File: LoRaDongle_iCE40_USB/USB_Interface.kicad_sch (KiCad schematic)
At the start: 25 parts, among them IC1 93LC56BT-I_OT, U2 FT232H, Y1 Crystal_GND24_Small

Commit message: updating unconnected traces
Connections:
- net UBS_D+ renamed USB_D+
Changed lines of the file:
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@@
     )
   )
-  (hierarchical_label "UBS_D+" (shape input) (at 140.97 58.42 180)
+  (hierarchical_label "USB_D+" (shape input) (at 140.97 58.42 180)
     (effects (font (size 1.27 1.27)) (justify right))
   )

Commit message: updating symbol details
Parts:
- C10: Manufacturer (none) -> Murata Electronics; Manufacturer Part Number (none) -> GRM155R71H103KA88J; Package (none) -> 0402; Type (none) -> SMD
- C11, C17, C7: footprint Capacitor_SMD:C_0603_1608Metric_Pad1.08x0.95mm_HandSolder -> Capacitor_SMD:C_0402_1005Metric_Pad0.74x0.62mm_HandSolder; Manufacturer (none) -> Murata Electronics; Manufacturer Part Number (none) -> GRM155C80J475MEAAD; Package (none) -> 0402; Type (none) -> SMD
- C12, C13, C16, C18, C19, C20, C21, C22, C8, C9: Manufacturer (none) -> Murata Electronics; Manufacturer Part Number (none) -> GCM155R71C104KA55J; Package (none) -> 0402; Type (none) -> SMD
- C14, C15: Manufacturer Part Number (none) -> Need to Find; Package (none) -> 0603; Type (none) -> SMD
- FB2, FB3: Manufacturer Part Number (none) -> BLM18AG601SN1D; Package (none) -> 0603; Type (none) -> SMD
- IC1: Manufacturer (none) -> Microchip; Manufacturer Part Number (none) -> 93LC56BT-I/OT; Package (none) -> SOT23-6; Type (none) -> SMD
- U2: Manufacturer (none) -> FTDI, Future Technology Devices International Ltd; Manufacturer Part Number (none) -> FT232HL; Package (none) -> LQFP-48; Type (none) -> SMD
- Y1: Manufacturer (none) -> Abracon LLC; Manufacturer Part Number (none) -> ABM8-12.000MHZ-B2-T; Package (none) -> 4 Pin Crystal; Type (none) -> SMD

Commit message: updated BOM
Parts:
- C14, C15: Manufacturer (none) -> Murata Electronics; Manufacturer Part Number Need to Find -> GRM1885C1H270JA01D
- R10, R8: Manufacturer (none) -> Stackpole Electronics Inc; Manufacturer Part Number (none) -> RMCF0402FT10K0
- R11: Manufacturer (none) -> Stackpole Electronics Inc; Manufacturer Part Number (none) -> RMCF0402FT12K0
- R9: Manufacturer (none) -> Stackpole Electronics Inc; Manufacturer Part Number (none) -> RMCF0402FT2K00
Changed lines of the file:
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@@
+      (effects (font (size 1.27 1.27)) hide)
+    )
+    (property "Description" "RES 10K OHM 1% 1/16W 0402" (id 4) (at 133.35 68.58 0)
+      (effects (font (size 1.27 1.27)) hide)
+    )
+    (property "Manufacturer" "Stackpole Electronics Inc" (id 5) (at 133.35 68.58 0)
+      (effects (font (size 1.27 1.27)) hide)
+    )
+    (property "Manufacturer Part Number" "RMCF0402FT12K0" (id 6) (at 133.35 68.58 0)
       (effects (font (size 1.27 1.27)) hide)
     )
@@
       (effects (font (size 1.27 1.27)) hide)
     )
+    (property "Description" "RES 2K OHM 1% 1/16W 0402" (id 4) (at 104.14 81.28 0)
+      (effects (font (size 1.27 1.27)) hide)
+    )
+    (property "Manufacturer" "Stackpole Electronics Inc" (id 5) (at 104.14 81.28 0)
+      (effects (font (size 1.27 1.27)) hide)
+    )
+    (property "Manufacturer Part Number" "RMCF0402FT2K00" (id 6) (at 104.14 81.28 0)
+      (effects (font (size 1.27 1.27)) hide)
+    )
     (pin "1")
     (pin "2")
@@
       (effects (font (size 1.27 1.27)) hide)
     )
+    (property "Description" "RES 10K OHM 1% 1/16W 0402" (id 4) (at 105.41 88.9 0)
+      (effects (font (size 1.27 1.27)) hide)
+    )
+    (property "Manufacturer" "Stackpole Electronics Inc" (id 5) (at 105.41 88.9 0)
+      (effects (font (size 1.27 1.27)) hide)
+    )
+    (property "Manufacturer Part Number" "RMCF0402FT10K0" (id 6) (at 105.41 88.9 0)
+      (effects (font (size 1.27 1.27)) hide)
+    )
     (pin "1")
     (pin "2")
@@
       (effects (font (size 1.27 1.27)) hide)
     )
-    (property "Manufacturer Part Number" "Need to Find " (id 4) (at 129.54 93.98 0)
+    (property "Manufacturer Part Number" "GRM1885C1H270JA01D" (id 4) (at 129.54 93.98 0)
       (effects (font (size 1.27 1.27)) hide)
     )
@@
     )
     (property "Type" "SMD" (id 6) (at 129.54 93.98 0)
+      (effects (font (size 1.27 1.27)) hide)
+    )
+    (property "Description" "CAP CER 27PF 50V C0G/NP0 0603" (id 7) (at 129.54 93.98 0)
+      (effects (font (size 1.27 1.27)) hide)
+    )
+    (property "Manufacturer" "Murata Electronics" (id 8) (at 129.54 93.98 0)
       (effects (font (size 1.27 1.27)) hide)
     )
@@
       (effects (font (size 1.27 1.27)) hide)
     )
-    (property "Manufacturer Part Number" "Need to Find " (id 4) (at 129.54 83.82 0)
+    (property "Manufacturer Part Number" "GRM1885C1H270JA01D" (id 4) (at 129.54 83.82 0)
       (effects (font (size 1.27 1.27)) hide)
     )
@@
     )
     (property "Type" "SMD" (id 6) (at 129.54 83.82 0)
+      (effects (font (size 1.27 1.27)) hide)
+    )
+    (property "Description" "CAP CER 27PF 50V C0G/NP0 0603" (id 7) (at 129.54 83.82 0)
+      (effects (font (size 1.27 1.27)) hide)
+    )
+    (property "Manufacturer" "Murata Electronics" (id 8) (at 129.54 83.82 0)
       (effects (font (size 1.27 1.27)) hide)
     )
@@
       (effects (font (size 1.27 1.27)) hide)
     )
+    (property "Description" "RES 10K OHM 1% 1/16W 0402" (id 4) (at 87.63 57.15 0)
+      (effects (font (size 1.27 1.27)) hide)
+    )
+    (property "Manufacturer" "Stackpole Electronics Inc" (id 5) (at 87.63 57.15 0)
+      (effects (font (size 1.27 1.27)) hide)
+    )
+    (property "Manufacturer Part Number" "RMCF0402FT10K0" (id 6) (at 87.63 57.15 0)
+      (effects (font (size 1.27 1.27)) hide)
+    )

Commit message: generate raw bom csv from kicad
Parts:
- R10, R11, R8, R9: Package (none) -> 0402
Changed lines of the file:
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@@
+      (effects (font (size 1.27 1.27)) hide)
+    )
+    (property "Package" "0402" (id 7) (at 133.35 68.58 0)
       (effects (font (size 1.27 1.27)) hide)
     )
@@
       (effects (font (size 1.27 1.27)) hide)
     )
+    (property "Package" "0402" (id 7) (at 104.14 81.28 0)
+      (effects (font (size 1.27 1.27)) hide)
+    )
     (pin "1")
     (pin "2")
@@
       (effects (font (size 1.27 1.27)) hide)
     )
+    (property "Package" "0402" (id 7) (at 105.41 88.9 0)
+      (effects (font (size 1.27 1.27)) hide)
+    )
     (pin "1")
     (pin "2")
@@
       (effects (font (size 1.27 1.27)) hide)
     )
+    (property "Package" "0402" (id 7) (at 87.63 57.15 0)
+      (effects (font (size 1.27 1.27)) hide)
+    )

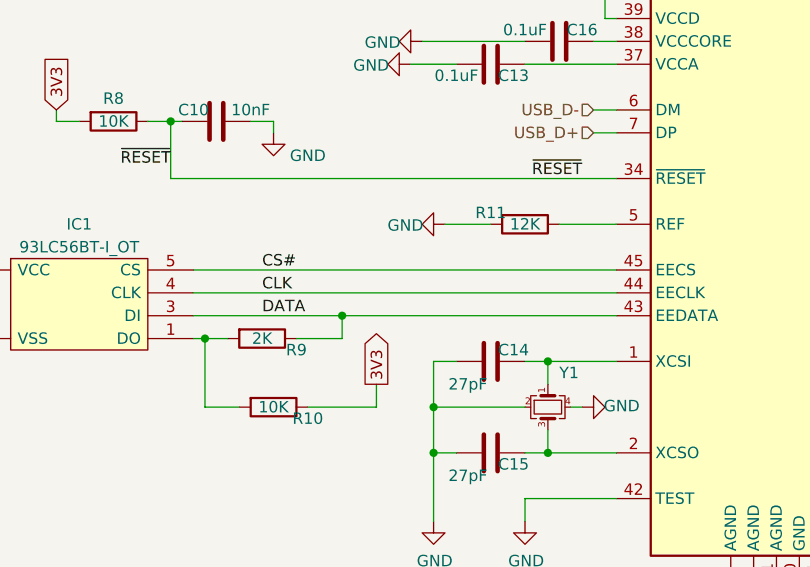
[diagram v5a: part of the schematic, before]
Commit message: added usb flash testpoints & jumper for fpga oscillator
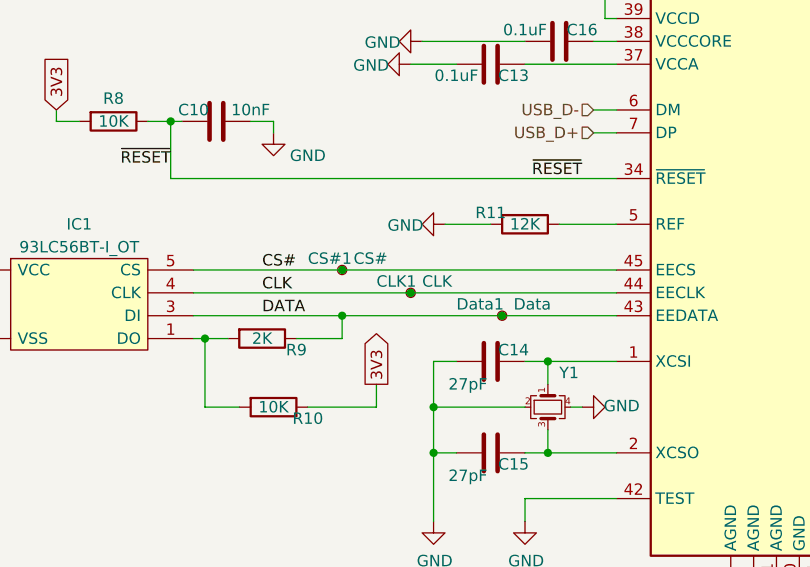
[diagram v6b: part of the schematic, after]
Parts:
- added CLK1: CLK, TestPoint:TestPoint_Pad_D1.0mm, symbol Connector:TestPoint_Small
- added CS#1: CS#, TestPoint:TestPoint_Pad_D1.0mm, symbol Connector:TestPoint_Small
- added Data1: Data, TestPoint:TestPoint_Pad_D1.0mm, symbol Connector:TestPoint_Small
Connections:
- net CLK: now also CLK1.1
- net CS#: now also CS#1.1
- net DATA: now also Data1.1
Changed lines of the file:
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@@
   (junction (at 172.72 144.78) (diameter 0) (color 0 0 0 0)
   )
+  (junction (at 120.65 76.2) (diameter 0) (color 0 0 0 0)
+  )
   (junction (at 64.77 73.66) (diameter 0) (color 0 0 0 0)
   )
@@
   (junction (at 142.24 40.64) (diameter 0) (color 0 0 0 0)
   )
+  (junction (at 135.89 93.98) (diameter 0) (color 0 0 0 0)
+  )
+  (junction (at 163.83 111.76) (diameter 0) (color 0 0 0 0)
+  )
+  (junction (at 166.37 111.76) (diameter 0) (color 0 0 0 0)
+  )
   (junction (at 113.03 78.74) (diameter 0) (color 0 0 0 0)
   )
-  (junction (at 135.89 93.98) (diameter 0) (color 0 0 0 0)
-  )
-  (junction (at 163.83 111.76) (diameter 0) (color 0 0 0 0)
-  )
-  (junction (at 166.37 111.76) (diameter 0) (color 0 0 0 0)
-  )
   (junction (at 168.91 111.76) (diameter 0) (color 0 0 0 0)
   )
+  (junction (at 130.81 78.74) (diameter 0) (color 0 0 0 0)
+  )
   (junction (at 118.11 144.78) (diameter 0) (color 0 0 0 0)
+  )
+  (junction (at 113.03 73.66) (diameter 0) (color 0 0 0 0)
   )
   (junction (at 158.75 111.76) (diameter 0) (color 0 0 0 0)
@@
     (stroke (width 0) (type default) (color 0 0 0 0))
   )
+  (wire (pts (xy 96.52 73.66) (xy 113.03 73.66))
+    (stroke (width 0) (type default) (color 0 0 0 0))
+  )
   (wire (pts (xy 187.96 144.78) (xy 189.23 144.78))
     (stroke (width 0) (type default) (color 0 0 0 0))
@@
     (stroke (width 0) (type default) (color 0 0 0 0))
   )
+  (wire (pts (xy 96.52 76.2) (xy 120.65 76.2))
+    (stroke (width 0) (type default) (color 0 0 0 0))
+  )
   (wire (pts (xy 133.35 99.06) (xy 143.51 99.06))
     (stroke (width 0) (type default) (color 0 0 0 0))
@@
     (stroke (width 0) (type default) (color 0 0 0 0))
   )
+  (wire (pts (xy 120.65 76.2) (xy 143.51 76.2))
+    (stroke (width 0) (type default) (color 0 0 0 0))
+  )
   (wire (pts (xy 156.21 109.22) (xy 156.21 111.76))
     (stroke (width 0) (type default) (color 0 0 0 0))
@@
     (stroke (width 0) (type default) (color 0 0 0 0))
   )
+  (wire (pts (xy 113.03 78.74) (xy 130.81 78.74))
+    (stroke (width 0) (type default) (color 0 0 0 0))
+  )
   (wire (pts (xy 124.46 68.58) (xy 129.54 68.58))
     (stroke (width 0) (type default) (color 0 0 0 0))
@@
     (stroke (width 0) (type default) (color 0 0 0 0))
   )
-  (wire (pts (xy 96.52 76.2) (xy 143.51 76.2))
-    (stroke (width 0) (type default) (color 0 0 0 0))
-  )
   (wire (pts (xy 143.51 58.42) (xy 140.97 58.42))
     (stroke (width 0) (type default) (color 0 0 0 0))
@@
     (stroke (width 0) (type default) (color 0 0 0 0))
   )
+  (wire (pts (xy 130.81 78.74) (xy 143.51 78.74))
+    (stroke (width 0) (type default) (color 0 0 0 0))
+  )
   (wire (pts (xy 172.72 144.78) (xy 181.61 144.78))
     (stroke (width 0) (type default) (color 0 0 0 0))
@@
     (stroke (width 0) (type default) (color 0 0 0 0))
   )
-  (wire (pts (xy 113.03 78.74) (xy 143.51 78.74))
-    (stroke (width 0) (type default) (color 0 0 0 0))
-  )
   (wire (pts (xy 96.52 81.28) (xy 97.79 81.28))
     (stroke (width 0) (type default) (color 0 0 0 0))
   )
-  (wire (pts (xy 96.52 73.66) (xy 143.51 73.66))
-    (stroke (width 0) (type default) (color 0 0 0 0))
-  )
   (wire (pts (xy 72.39 144.78) (xy 68.58 144.78))
     (stroke (width 0) (type default) (color 0 0 0 0))
@@
   )
   (wire (pts (xy 41.91 132.08) (xy 41.91 134.62))
+    (stroke (width 0) (type default) (color 0 0 0 0))
+  )
+  (wire (pts (xy 113.03 73.66) (xy 143.51 73.66))
     (stroke (width 0) (type default) (color 0 0 0 0))
   )
@@
       (effects (font (size 1.27 1.27)) hide)
     )
+    (pin "1")
+  )
+  (symbol (lib_id "Connector:TestPoint_Small") (at 113.03 73.66 0) (unit 1)
+    (in_bom yes) (on_board yes)
+    (property "Reference" "CS#1" (id 0) (at 109.22 72.39 0)
+      (effects (font (size 1.27 1.27)) (justify left))
+    )
+    (property "Value" "CS#" (id 1) (at 114.3 72.39 0)
+      (effects (font (size 1.27 1.27)) (justify left))
+    )
+    (property "Footprint" "TestPoint:TestPoint_Pad_D1.0mm" (id 2) (at 118.11 73.66 0)
+      (effects (font (size 1.27 1.27)) hide)
+    )
+    (property "Datasheet" "~" (id 3) (at 118.11 73.66 0)
+      (effects (font (size 1.27 1.27)) hide)
+    )
+    (pin "1")
+  )
+  (symbol (lib_id "Connector:TestPoint_Small") (at 130.81 78.74 0) (unit 1)
+    (in_bom yes) (on_board yes)
+    (property "Reference" "Data1" (id 0) (at 125.73 77.47 0)
+      (effects (font (size 1.27 1.27)) (justify left))
+    )
+    (property "Value" "Data" (id 1) (at 132.08 77.47 0)
+      (effects (font (size 1.27 1.27)) (justify left))
+    )
+    (property "Footprint" "TestPoint:TestPoint_Pad_D1.0mm" (id 2) (at 135.89 78.74 0)
+      (effects (font (size 1.27 1.27)) hide)
+    )
+    (property "Datasheet" "~" (id 3) (at 135.89 78.74 0)
+      (effects (font (size 1.27 1.27)) hide)
+    )
+    (pin "1")
+  )
+  (symbol (lib_id "Connector:TestPoint_Small") (at 120.65 76.2 0) (unit 1)
+    (in_bom yes) (on_board yes)
+    (property "Reference" "CLK1" (id 0) (at 116.84 74.93 0)
+      (effects (font (size 1.27 1.27)) (justify left))
+    )
+    (property "Value" "CLK" (id 1) (at 121.92 74.93 0)
+      (effects (font (size 1.27 1.27)) (justify left))
+    )
+    (property "Footprint" "TestPoint:TestPoint_Pad_D1.0mm" (id 2) (at 125.73 76.2 0)
+      (effects (font (size 1.27 1.27)) hide)
+    )
+    (property "Datasheet" "~" (id 3) (at 125.73 76.2 0)
+      (effects (font (size 1.27 1.27)) hide)
+    )

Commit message: updating silkscreen
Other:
- company: (none) -> Mark Njoroge
- title: (none) -> RiscVLoRaDongle
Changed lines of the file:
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@@
 (kicad_sch (version 20211123) (generator eeschema)
   (paper "A4")
+  (title_block
+    (title "RiscVLoRaDongle")
+    (date "2022-02-03")
+    (rev "1.0")
+    (company "Mark Njoroge")
+  )
   (junction (at 64.77 81.28) (diameter 0) (color 0 0 0 0)
   )
@@
   (junction (at 146.05 134.62) (diameter 0) (color 0 0 0 0)
   )
+  (junction (at 120.65 134.62) (diameter 0) (color 0 0 0 0)
+  )
   (junction (at 113.03 134.62) (diameter 0) (color 0 0 0 0)
   )
@@
   )
   (junction (at 154.94 144.78) (diameter 0) (color 0 0 0 0)
+  )
+  (junction (at 68.58 134.62) (diameter 0) (color 0 0 0 0)
+  )
+  (junction (at 161.29 134.62) (diameter 0) (color 0 0 0 0)
   )
   (junction (at 93.98 57.15) (diameter 0) (color 0 0 0 0)
@@
     (stroke (width 0) (type default) (color 0 0 0 0))
   )
+  (wire (pts (xy 120.65 134.62) (xy 113.03 134.62))
+    (stroke (width 0) (type default) (color 0 0 0 0))
+  )
   (wire (pts (xy 143.51 45.72) (xy 142.24 45.72))
     (stroke (width 0) (type default) (color 0 0 0 0))
@@
     (stroke (width 0) (type default) (color 0 0 0 0))
   )
-  (wire (pts (xy 154.94 134.62) (xy 163.83 134.62))
+  (wire (pts (xy 154.94 134.62) (xy 161.29 134.62))
     (stroke (width 0) (type default) (color 0 0 0 0))
   )
@@
     (stroke (width 0) (type default) (color 0 0 0 0))
   )
-  (wire (pts (xy 72.39 134.62) (xy 63.5 134.62))
+  (wire (pts (xy 72.39 134.62) (xy 68.58 134.62))
     (stroke (width 0) (type default) (color 0 0 0 0))
   )
@@
     (stroke (width 0) (type default) (color 0 0 0 0))
   )
+  (wire (pts (xy 161.29 134.62) (xy 163.83 134.62))
+    (stroke (width 0) (type default) (color 0 0 0 0))
+  )
   (wire (pts (xy 68.58 144.78) (xy 68.58 147.32))
     (stroke (width 0) (type default) (color 0 0 0 0))
@@
     (stroke (width 0) (type default) (color 0 0 0 0))
   )
-  (wire (pts (xy 121.92 134.62) (xy 113.03 134.62))
+  (wire (pts (xy 121.92 134.62) (xy 120.65 134.62))
     (stroke (width 0) (type default) (color 0 0 0 0))
   )
@@
   )
   (wire (pts (xy 64.77 81.28) (xy 64.77 83.82))
+    (stroke (width 0) (type default) (color 0 0 0 0))
+  )
+  (wire (pts (xy 68.58 134.62) (xy 63.5 134.62))
     (stroke (width 0) (type default) (color 0 0 0 0))
   )
@@
   (label "~{RESET}" (at 93.98 62.23 180)
     (effects (font (size 1.27 1.27)) (justify right bottom))
-  )
-  (label "FT232" (at 148.59 134.62 0)
-    (effects (font (size 1.27 1.27)) (justify left bottom))
-  )
-  (label "FT232" (at 171.45 30.48 0)
-    (effects (font (size 1.27 1.27)) (justify left bottom))
   )
   (label "CLK" (at 104.14 76.2 0)
@@
       (effects (font (size 1.27 1.27)) hide)
     )
+    (pin "1")
+  )
+  (symbol (lib_id "power:PWR_FLAG") (at 120.65 134.62 0) (unit 1)
+    (in_bom yes) (on_board yes)
+    (property "Reference" "#FLG06" (id 0) (at 120.65 132.715 0)
+      (effects (font (size 1.27 1.27)) hide)
+    )
+    (property "Value" "PWR_FLAG" (id 1) (at 127 133.35 0))
+    (property "Footprint" "" (id 2) (at 120.65 134.62 0)
+      (effects (font (size 1.27 1.27)) hide)
+    )
+    (property "Datasheet" "~" (id 3) (at 120.65 134.62 0)
+      (effects (font (size 1.27 1.27)) hide)
+    )
+    (pin "1")
+  )
+  (symbol (lib_id "power:PWR_FLAG") (at 68.58 134.62 0) (unit 1)
+    (in_bom yes) (on_board yes)
+    (property "Reference" "#FLG05" (id 0) (at 68.58 132.715 0)
+      (effects (font (size 1.27 1.27)) hide)
+    )
+    (property "Value" "PWR_FLAG" (id 1) (at 74.93 133.35 0))
+    (property "Footprint" "" (id 2) (at 68.58 134.62 0)
+      (effects (font (size 1.27 1.27)) hide)
+    )
+    (property "Datasheet" "~" (id 3) (at 68.58 134.62 0)
+      (effects (font (size 1.27 1.27)) hide)
+    )
+    (pin "1")
+  )
+  (symbol (lib_id "power:PWR_FLAG") (at 161.29 134.62 0) (unit 1)
+    (in_bom yes) (on_board yes) (fields_autoplaced)
+    (property "Reference" "#FLG0101" (id 0) (at 161.29 132.715 0)
+      (effects (font (size 1.27 1.27)) hide)
+    )
+    (property "Value" "PWR_FLAG" (id 1) (at 161.29 129.54 0))
+    (property "Footprint" "" (id 2) (at 161.29 134.62 0)
+      (effects (font (size 1.27 1.27)) hide)
+    )
+    (property "Datasheet" "~" (id 3) (at 161.29 134.62 0)
+      (effects (font (size 1.27 1.27)) hide)
+    )

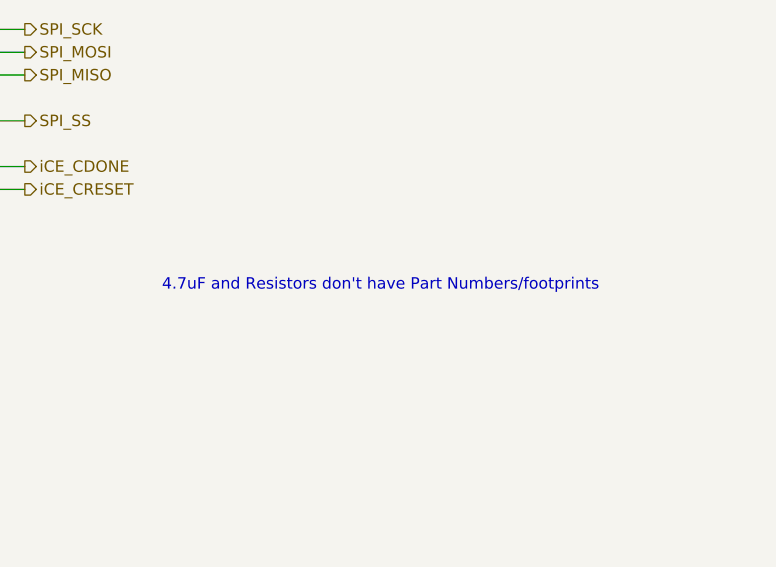
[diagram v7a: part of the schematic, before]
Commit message: updating text in schematic
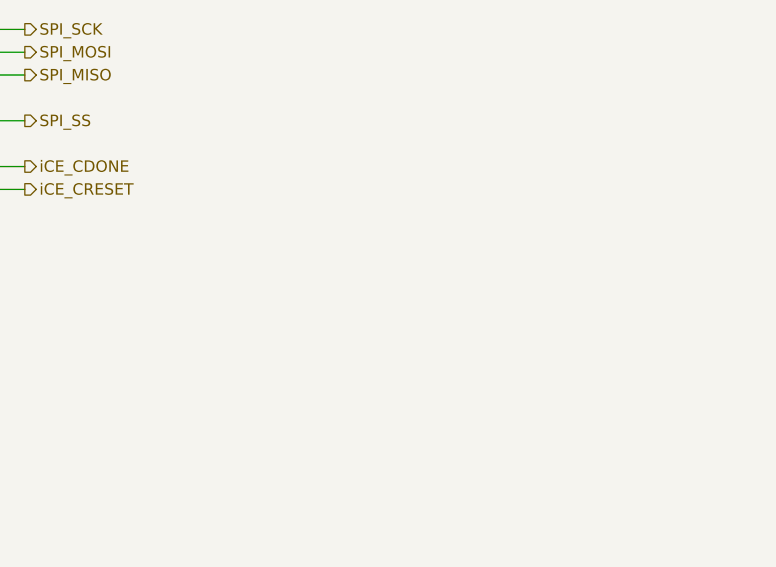
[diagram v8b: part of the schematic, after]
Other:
- note removed: "4.7uF and Resistors don't have Part Numbers/footprints"
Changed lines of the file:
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@@
     (stroke (width 0) (type default) (color 0 0 0 0))
-  )
-  (text "4.7uF and Resistors don't have Part Numbers/footprints"
-    (at 215.9 69.85 0)
-    (effects (font (size 1.27 1.27)) (justify left bottom))
   )
   (text "Connect the LC circuits for VPHY and VLL" (at 72.39 124.46 0)
